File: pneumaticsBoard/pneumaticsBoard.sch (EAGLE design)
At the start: 48 parts, among them IC1 MAX232, Q1 BSS296, Q2 BSS296, Q3 BSS296, Q4 BSS296, Q5 BSS296, Q6 BSS296, Q7 BSS296, Q8 BSS296, U1 ATMEGA328P-PU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

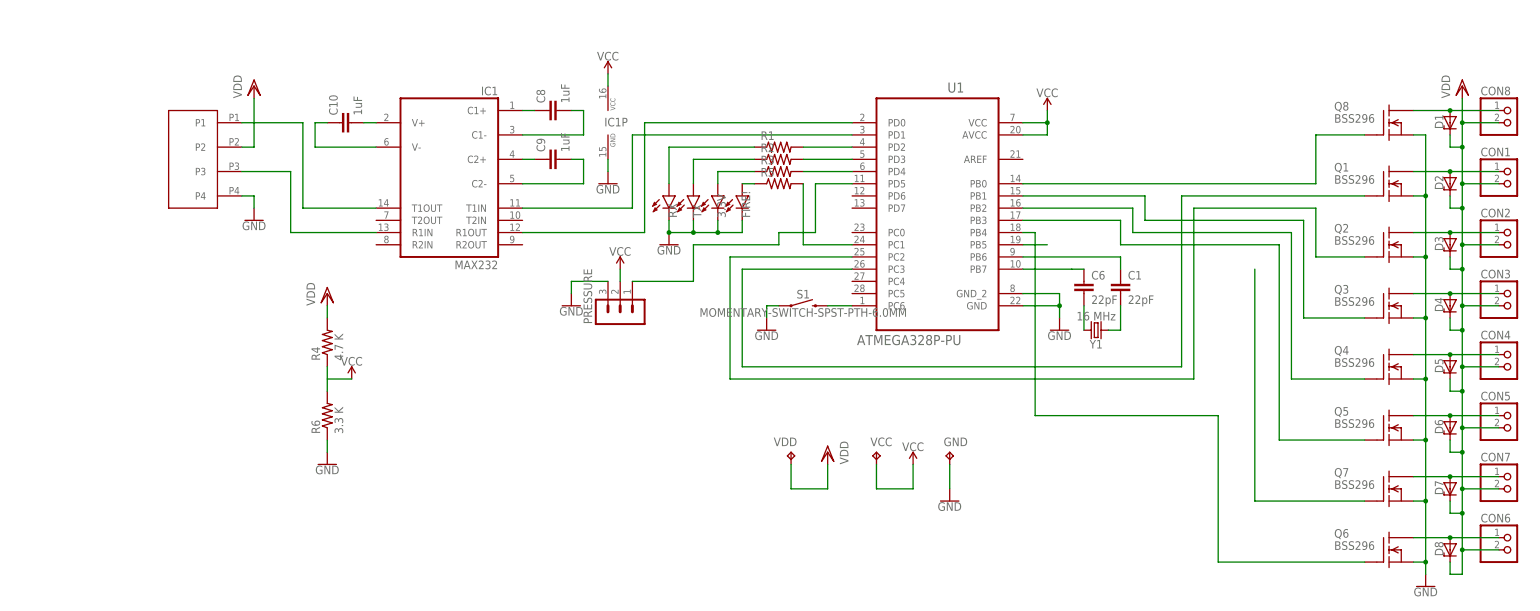
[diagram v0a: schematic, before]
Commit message: Pneumatics Board complete. Gerber files uploaded.
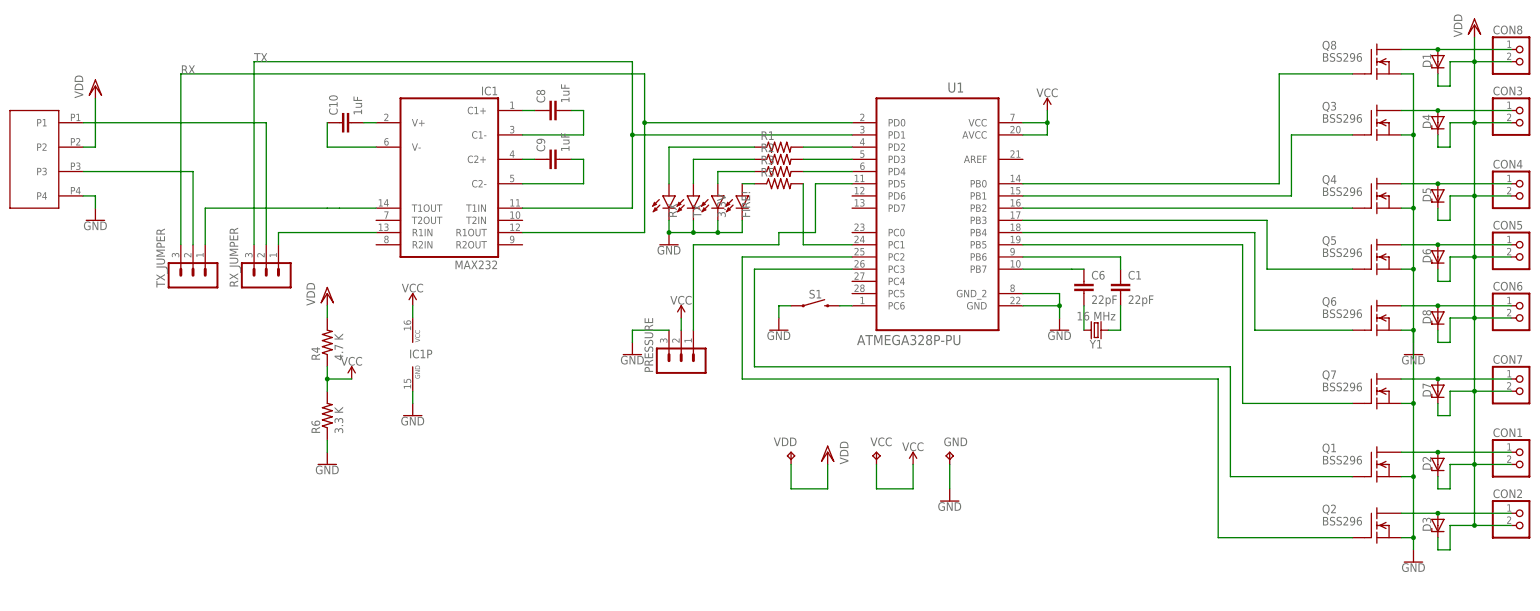
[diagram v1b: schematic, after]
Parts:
- added RX_JUMPER, TX_JUMPER: (no value), con-lstb:MA03-1
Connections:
- removed net RS232_RX-ATMEGA_TX: IC1G$1.R1OUT, U1.PD0
- removed net RS232_TX-ATMEGA_RX: IC1G$1.T1IN, U1.PD1
- new net N$16: IC1G$1.R1IN, RX_JUMPER.1
- new net RX_ORIGINAL: RX_JUMPER.2, U$2.P1
- new net TX_ORIGINAL: TX_JUMPER.2, U$2.P3
- net N$3: now also IC1G$1.T1OUT, TX_JUMPER.1; no longer R4.1, R6.2
- net RX: now also IC1G$1.R1OUT, TX_JUMPER.3, U1.PD0; no longer IC1G$1.R1IN, U$2.P3
- net TX: now also IC1G$1.T1IN, RX_JUMPER.3, U1.PD1; no longer IC1G$1.T1OUT, U$2.P1
- net VCC: now also R4.1, R6.2
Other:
- moved on the sheet: CON1, CON2, CON3, CON4, CON5, CON6, CON7, CON8, D1, D2, D3, D4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

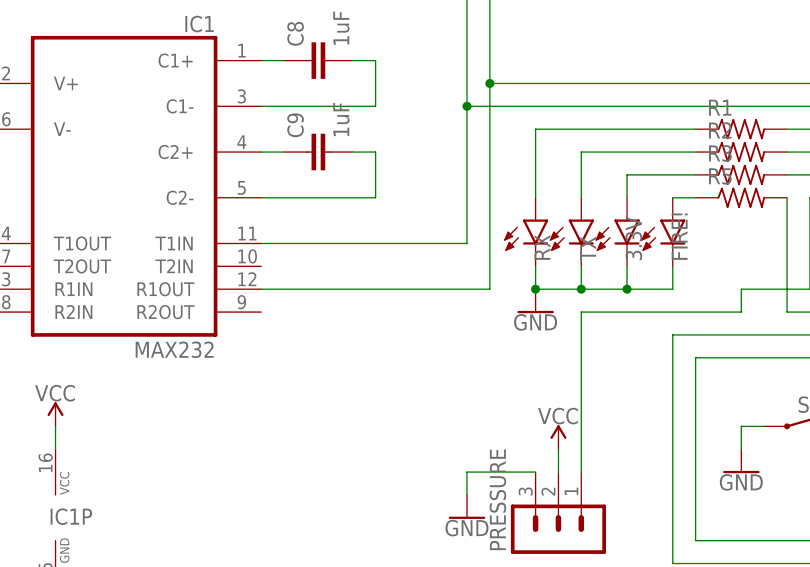
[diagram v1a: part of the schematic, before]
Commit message: Added 0 Ohm Resistors on TX and RX lines just in case.
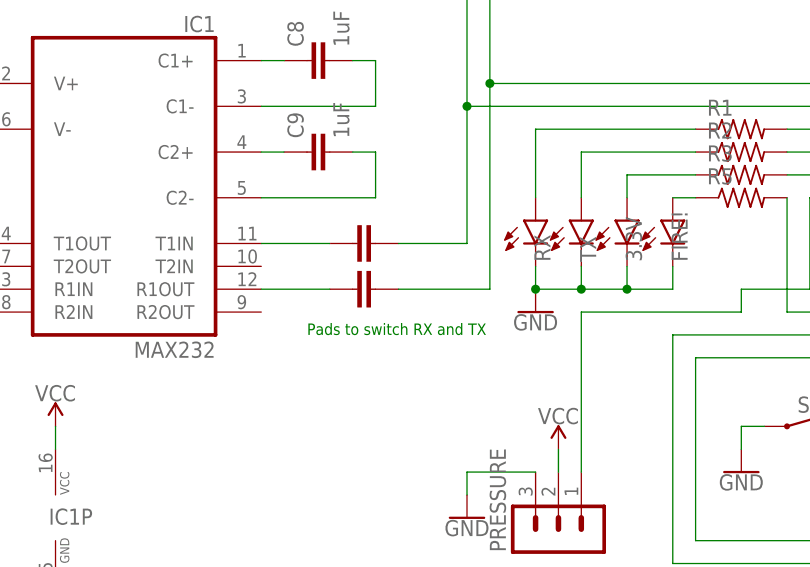
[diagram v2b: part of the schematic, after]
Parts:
- added C2, C3: 1uF, SparkFun-Capacitors:470PF-0603-50V-5%
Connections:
- new net N$17: C2.1, IC1G$1.T1IN
- new net N$18: C3.1, IC1G$1.R1OUT
- net RX: now also C3.2; no longer IC1G$1.R1OUT
- net TX: now also C2.2; no longer IC1G$1.T1IN
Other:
- note added: "Pads to switch RX and TX"
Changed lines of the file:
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@@
 <part name="TX_JUMPER" library="con-lstb" library_urn="urn:adsk.eagle:library:162" deviceset="MA03-1" device="" package3d_urn="urn:adsk.eagle:package:8339/1"/>
 <part name="RX_JUMPER" library="con-lstb" library_urn="urn:adsk.eagle:library:162" deviceset="MA03-1" device="" package3d_urn="urn:adsk.eagle:package:8339/1"/>
+<part name="C2" library="SparkFun-Capacitors" deviceset="470PF" device="-0603-50V-5%" value="1uF"/>
+<part name="C3" library="SparkFun-Capacitors" deviceset="470PF" device="-0603-50V-5%" value="1uF"/>
 </parts>
 <sheets>
 <sheet>
 <plain>
+<text x="-63.5" y="30.48" size="1.27" layer="91">Pads to switch RX and TX</text>
 </plain>
 <instances>
@@
 <instance part="TX_JUMPER" gate="G$1" x="-137.16" y="25.4" rot="R90"/>
 <instance part="RX_JUMPER" gate="G$1" x="-121.92" y="25.4" rot="R90"/>
+<instance part="C2" gate="G$1" x="-55.88" y="40.64" smashed="yes" rot="R90"/>
+<instance part="C3" gate="G$1" x="-55.88" y="35.56" smashed="yes" rot="R90"/>
 </instances>
 <busses>
@@
 <segment>
 <wire x1="-43.18" y1="58.42" x2="-43.18" y2="35.56" width="0.1524" layer="91"/>
-<pinref part="IC1" gate="G$1" pin="R1OUT"/>
-<wire x1="-68.58" y1="35.56" x2="-43.18" y2="35.56" width="0.1524" layer="91"/>
 <pinref part="U1" gate="A" pin="PD0"/>
+<wire x1="-53.34" y1="35.56" x2="-43.18" y2="35.56" width="0.1524" layer="91"/>
 <wire x1="0" y1="58.42" x2="-43.18" y2="58.42" width="0.1524" layer="91"/>
 <wire x1="-43.18" y1="68.58" x2="-43.18" y2="58.42" width="0.1524" layer="91"/>
@@
 <wire x1="-43.18" y1="68.58" x2="-139.7" y2="68.58" width="0.1524" layer="91"/>
 <label x="-139.7" y="68.58" size="1.778" layer="95"/>
+<pinref part="C3" gate="G$1" pin="2"/>
 </segment>
 </net>
@@
 <net name="TX" class="0">
 <segment>
-<pinref part="IC1" gate="G$1" pin="T1IN"/>
 <wire x1="-45.72" y1="55.88" x2="-45.72" y2="40.64" width="0.1524" layer="91"/>
-<wire x1="-45.72" y1="40.64" x2="-68.58" y2="40.64" width="0.1524" layer="91"/>
+<wire x1="-45.72" y1="40.64" x2="-53.34" y2="40.64" width="0.1524" layer="91"/>
 <pinref part="U1" gate="A" pin="PD1"/>
 <wire x1="0" y1="55.88" x2="-45.72" y2="55.88" width="0.1524" layer="91"/>
@@
 <wire x1="-124.46" y1="33.02" x2="-124.46" y2="71.12" width="0.1524" layer="91"/>
 <label x="-124.46" y="71.12" size="1.778" layer="95"/>
-</segment>
-</net>
+<pinref part="C2" gate="G$1" pin="2"/>
+</segment>
+</net>
+<net name="N$17" class="0">
+<segment>
+<pinref part="IC1" gate="G$1" pin="T1IN"/>
+<wire x1="-60.96" y1="40.64" x2="-68.58" y2="40.64" width="0.1524" layer="91"/>
+<pinref part="C2" gate="G$1" pin="1"/>
+</segment>
+</net>
+<net name="N$18" class="0">
+<segment>
+<pinref part="IC1" gate="G$1" pin="R1OUT"/>
+<wire x1="-68.58" y1="35.56" x2="-60.96" y2="35.56" width="0.1524" layer="91"/>
+<pinref part="C3" gate="G$1" pin="1"/>
+</segment>
+</net>

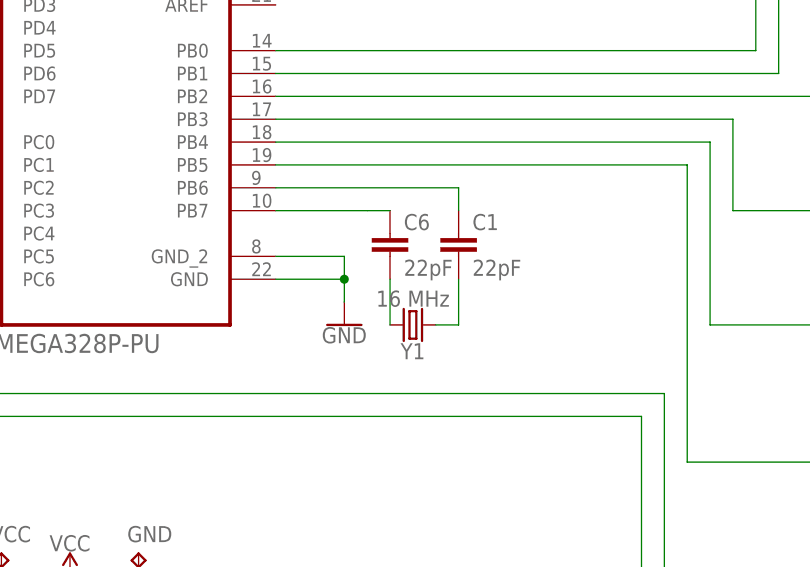
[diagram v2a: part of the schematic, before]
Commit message: Crystal Circuit wasn't grounded
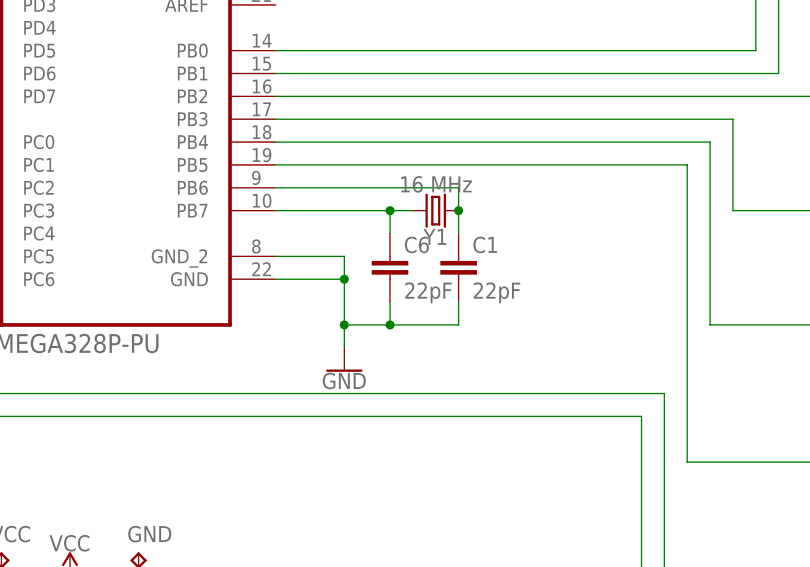
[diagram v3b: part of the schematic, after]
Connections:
- removed net N$15: C1.2, Y1.1
- removed net N$5: C6.2, Y1.2
- net GND: now also C1.2, C6.2
- net XTAL1: now also Y1.1
- net XTAL2: now also Y1.2
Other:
- moved on the sheet: C1, C6, Y1
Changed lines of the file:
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@@
 <attribute name="NAME" x="-7.62" y="21.844" size="1.778" layer="95" font="vector" align="bottom-center"/>
 </instance>
-<instance part="Y1" gate="G$1" x="50.8" y="15.24" rot="R180"/>
+<instance part="Y1" gate="G$1" x="53.34" y="27.94" rot="R180"/>
 <instance part="CON1" gate="G$1" x="139.7" y="-12.7"/>
 <instance part="CON2" gate="G$1" x="139.7" y="-25.4"/>
@@
 <instance part="GND1" gate="1" x="-91.44" y="-2.54"/>
 <instance part="GND2" gate="1" x="-15.24" y="15.24"/>
-<instance part="GND3" gate="1" x="43.18" y="15.24"/>
+<instance part="GND3" gate="1" x="43.18" y="10.16"/>
 <instance part="VDD1" gate="G$1" x="129.54" y="78.74"/>
 <instance part="VDD2" gate="G$1" x="-157.48" y="66.04"/>
@@
 <instance part="GND7" gate="1" x="-157.48" y="38.1"/>
 <instance part="GND8" gate="1" x="116.84" y="10.16"/>
-<instance part="C6" gate="G$1" x="48.26" y="22.86"/>
+<instance part="C6" gate="G$1" x="48.26" y="20.32"/>
 <instance part="C8" gate="G$1" x="-60.96" y="60.96" rot="R90"/>
 <instance part="C9" gate="G$1" x="-60.96" y="50.8" rot="R90"/>
 <instance part="C10" gate="G$1" x="-104.14" y="58.42" rot="R90"/>
-<instance part="C1" gate="G$1" x="55.88" y="22.86"/>
+<instance part="C1" gate="G$1" x="55.88" y="20.32"/>
 <instance part="PRESSURE" gate="G$1" x="-35.56" y="7.62" rot="R90"/>
 <instance part="SUPPLY5" gate="G$1" x="-35.56" y="17.78"/>
@@
 <pinref part="U1" gate="A" pin="PB6"/>
 <wire x1="35.56" y1="30.48" x2="55.88" y2="30.48" width="0.1524" layer="91"/>
-<wire x1="55.88" y1="30.48" x2="55.88" y2="27.94" width="0.1524" layer="91"/>
+<pinref part="Y1" gate="G$1" pin="1"/>
 <pinref part="C1" gate="G$1" pin="1"/>
+<wire x1="55.88" y1="27.94" x2="55.88" y2="25.4" width="0.1524" layer="91"/>
+<wire x1="55.88" y1="27.94" x2="55.88" y2="30.48" width="0.1524" layer="91"/>
+<junction x="55.88" y="27.94"/>
 </segment>
 </net>
@@
 <segment>
 <pinref part="U1" gate="A" pin="PB7"/>
-<wire x1="35.56" y1="27.94" x2="45.72" y2="27.94" width="0.1524" layer="91"/>
-<wire x1="48.26" y1="27.94" x2="45.72" y2="27.94" width="0.1524" layer="91"/>
+<wire x1="35.56" y1="27.94" x2="48.26" y2="27.94" width="0.1524" layer="91"/>
 <pinref part="C6" gate="G$1" pin="1"/>
+<wire x1="48.26" y1="27.94" x2="48.26" y2="25.4" width="0.1524" layer="91"/>
+<pinref part="Y1" gate="G$1" pin="2"/>
+<wire x1="48.26" y1="27.94" x2="50.8" y2="27.94" width="0.1524" layer="91"/>
+<junction x="48.26" y="27.94"/>
 </segment>
 </net>
@@
 <wire x1="35.56" y1="20.32" x2="43.18" y2="20.32" width="0.1524" layer="91"/>
 <wire x1="43.18" y1="20.32" x2="43.18" y2="22.86" width="0.1524" layer="91"/>
-<wire x1="43.18" y1="20.32" x2="43.18" y2="17.78" width="0.1524" layer="91"/>
+<wire x1="43.18" y1="20.32" x2="43.18" y2="15.24" width="0.1524" layer="91"/>
 <junction x="43.18" y="20.32"/>
 <pinref part="GND3" gate="1" pin="GND"/>
+<pinref part="C6" gate="G$1" pin="2"/>
+<wire x1="43.18" y1="15.24" x2="43.18" y2="12.7" width="0.1524" layer="91"/>
+<wire x1="48.26" y1="17.78" x2="48.26" y2="15.24" width="0.1524" layer="91"/>
+<pinref part="C1" gate="G$1" pin="2"/>
+<wire x1="48.26" y1="15.24" x2="55.88" y2="15.24" width="0.1524" layer="91"/>
+<wire x1="55.88" y1="15.24" x2="55.88" y2="17.78" width="0.1524" layer="91"/>
+<wire x1="48.26" y1="15.24" x2="43.18" y2="15.24" width="0.1524" layer="91"/>
+<junction x="48.26" y="15.24"/>
+<junction x="43.18" y="15.24"/>
 </segment>
 <segment>
@@
 </segment>
 </net>
-<net name="N$5" class="0">
-<segment>
-<pinref part="C6" gate="G$1" pin="2"/>
-<pinref part="Y1" gate="G$1" pin="2"/>
-<wire x1="48.26" y1="20.32" x2="48.26" y2="15.24" width="0.1524" layer="91"/>
-</segment>
-</net>
-<net name="N$15" class="0">
-<segment>
-<pinref part="Y1" gate="G$1" pin="1"/>
-<wire x1="55.88" y1="20.32" x2="55.88" y2="15.24" width="0.1524" layer="91"/>
-<wire x1="55.88" y1="15.24" x2="53.34" y2="15.24" width="0.1524" layer="91"/>
-<pinref part="C1" gate="G$1" pin="2"/>
-</segment>
-</net>

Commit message: PN - changed VD to Reg, added pressure sensor, added silkscreen to proper layer
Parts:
- removed PRESSURE: (no value), con-lstb:MA03-1
- removed R4: 4.7 K, resistor:R-US_0204/2V
- removed R6: 3.3 K, resistor:R-US_0204/2V
- added PRESSURE_SENSOR: (no value), ic-package:DIL8
- added U$1: L78M05CV, L78M05CV:L78M05CV
- Q1, Q2, Q3, Q4, Q5, Q6, Q7, Q8: value BSS296 -> 60V/32A/35mΩ; device transistor-fet:BSS296 -> SparkFun-DiscreteSemi:MOSFET-NCH-FQP30N06L
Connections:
- removed net N$6: PRESSURE.1, U1.PD5
- new net PRESSURE: PRESSURE_SENSOR.2, U1.PC0
- net GND: now also PRESSURE_SENSOR.3, U$1.GND; no longer PRESSURE.3, R6.1
- net VCC: now also PRESSURE_SENSOR.1, U$1.OUTPUT; no longer PRESSURE.2, R4.1, R6.2
- net VDD: now also U$1.INPUT; no longer R4.2
